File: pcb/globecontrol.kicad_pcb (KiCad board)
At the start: 2 copper layers, 17.8 x 30.2 mm, 11 parts, among them J1 SLIPRING, J2 HOME, J3 SERVO, J4 LASER, Q1 MMBT2222A, U1 AMS1117-3.3

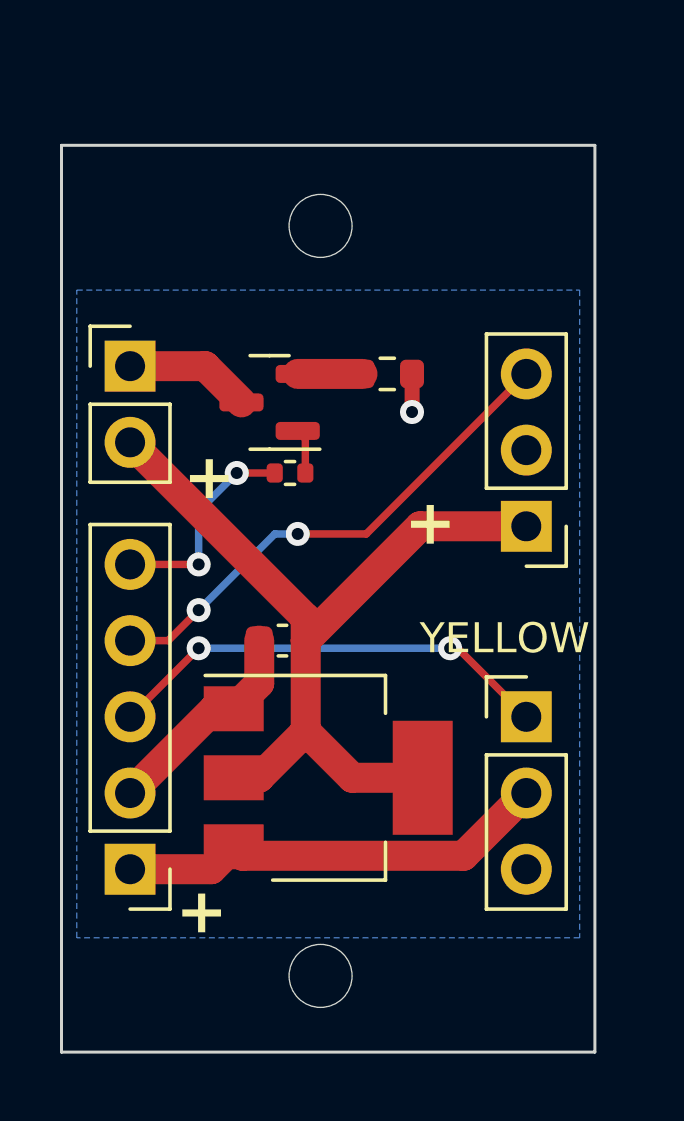
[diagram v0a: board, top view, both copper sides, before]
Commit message: Added control for an LED for internal illumination
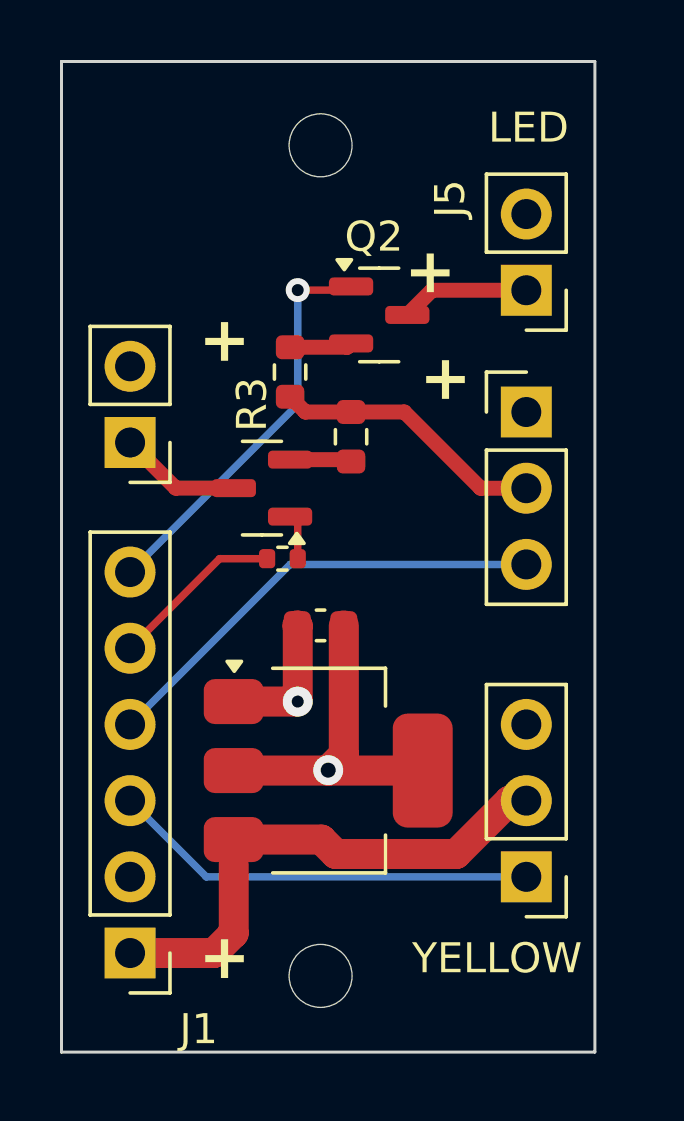
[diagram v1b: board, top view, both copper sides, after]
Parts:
- added J5: LASER, Connector_PinHeader_2.54mm:PinHeader_1x02_P2.54mm_Vertical, F.Cu at (142.5, 76.5)
- added Q2: MMBT2222A, Package_TO_SOT_SMD:SOT-23, F.Cu at (137.6, 77.3)
- added R3: 33, Resistor_SMD:R_0603_1608Metric, F.Cu at (134.6, 79.2)
- J1: value SLIPRING -> Conn_01x06_Pin; footprint Connector_PinHeader_2.54mm:PinHeader_1x05_P2.54mm_Vertical -> Connector_PinHeader_2.54mm:PinHeader_1x06_P2.54mm_Vertical
- moved J3 5.33 mm to (142.5, 96.0), turned to 180 degrees
- moved J2 3.81 mm to (142.5, 80.5), turned to 0 degrees
- moved Q1 2.87 mm to (133.7, 83.1)
- moved R1 2.87 mm to (134.4, 85.4)
- moved J1 2.79 mm to (129.3, 98.6)
- moved H1 2.69 mm to (135.6, 71.6)
- moved J4 2.55 mm to (129.3, 81.5), turned to 180 degrees
- moved R2 2.42 mm to (136.7, 81.3), turned to -90 degrees
- moved C1 1.37 mm to (135.6, 87.6)
- moved U1 0.24 mm to (135.9, 92.5)
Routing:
- net +3V3: track 28.6 -> 11.4 mm, vias 0 -> 1
- net LED: track 0.00 -> 13.5 mm, vias 0 -> 1
- net GND: track 8.51 -> 14.1 mm
- net Net-(J5-Pin_1): track 0.00 -> 4.31 mm
- net +5V: track 14.5 -> 16.7 mm
- net Net-(Q2-E): track 0.00 -> 2.09 mm
- net ZERO: track 16.9 -> 15.4 mm, vias 2 -> 0
- net LASER: track 7.13 -> 5.80 mm, vias 2 -> 0
- net SERVO: track 15.1 -> 14.5 mm, vias 2 -> 0
- added copper zone on In2.Cu, net +3V3
- added copper zone on In1.Cu, net GND
- removed copper zone on B.Cu, net GND
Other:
- board size 17.8 x 30.2 mm -> 17.8 x 33 mm
- copper layers 2 -> 4
- board text added: "LED"
- board text added: "Router V3 May, 2024"
- board text removed: "Router V2.1"
